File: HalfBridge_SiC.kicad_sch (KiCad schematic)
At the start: 0 parts

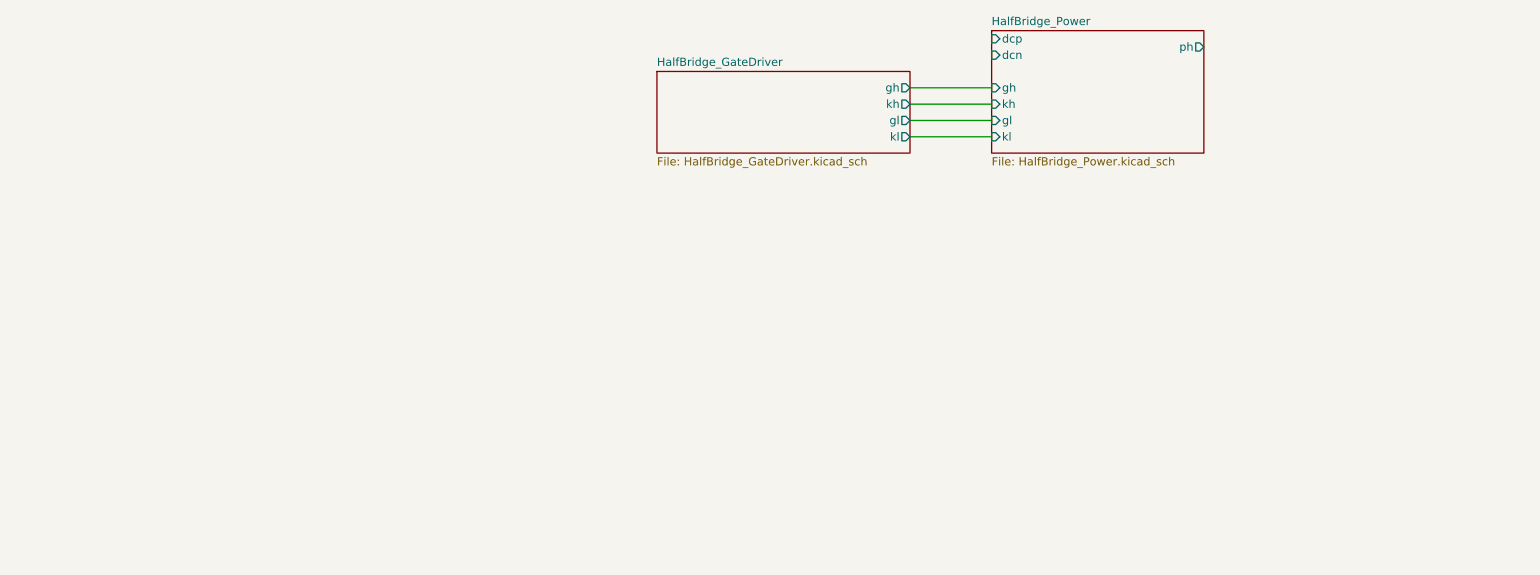
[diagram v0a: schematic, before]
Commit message: gate driver
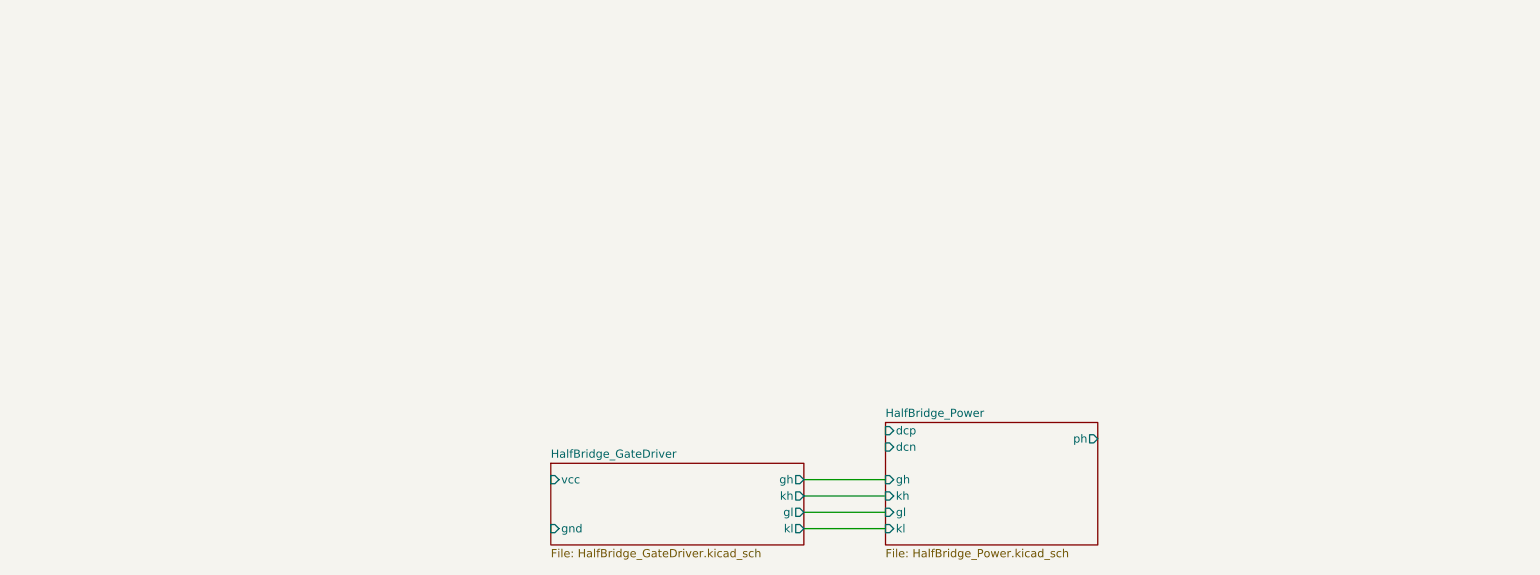
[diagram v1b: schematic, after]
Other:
- sheet HalfBridge_GateDriver ports: added gnd, vcc; removed none
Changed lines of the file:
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@@
 	(wire
 		(pts
-			(xy 132.08 63.5) (xy 144.78 63.5)
-		)
-		(stroke
-			(width 0)
-			(type default)
-		)
-	)
-	(wire
-		(pts
-			(xy 132.08 58.42) (xy 144.78 58.42)
-		)
-		(stroke
-			(width 0)
-			(type default)
-		)
-	)
-	(wire
-		(pts
-			(xy 132.08 60.96) (xy 144.78 60.96)
-		)
-		(stroke
-			(width 0)
-			(type default)
-		)
-	)
-	(wire
-		(pts
-			(xy 132.08 55.88) (xy 144.78 55.88)
+			(xy 115.57 124.46) (xy 128.27 124.46)
+		)
+		(stroke
+			(width 0)
+			(type default)
+		)
+	)
+	(wire
+		(pts
+			(xy 115.57 119.38) (xy 128.27 119.38)
+		)
+		(stroke
+			(width 0)
+			(type default)
+		)
+	)
+	(wire
+		(pts
+			(xy 115.57 121.92) (xy 128.27 121.92)
+		)
+		(stroke
+			(width 0)
+			(type default)
+		)
+	)
+	(wire
+		(pts
+			(xy 115.57 116.84) (xy 128.27 116.84)
 		)
 		(stroke
@@
 	)
 	(sheet
-		(at 92.71 53.34)
+		(at 76.2 114.3)
 		(size 39.37 12.7)
 		(fields_autoplaced yes)
@@
 		)
 		(property "Sheetname" "HalfBridge_GateDriver"
-			(at 92.71 52.6284 0)
+			(at 76.2 113.5884 0)
 			(effects
 				(font
@@
 		)
 		(property "Sheetfile" "HalfBridge_GateDriver.kicad_sch"
-			(at 92.71 66.6246 0)
+			(at 76.2 127.5846 0)
 			(effects
 				(font
@@
 		)
 		(pin "gl" output
-			(at 132.08 60.96 0)
+			(at 115.57 121.92 0)
 			(effects
 				(font
@@
 		)
 		(pin "kh" output
-			(at 132.08 58.42 0)
+			(at 115.57 119.38 0)
 			(effects
 				(font
@@
 		)
 		(pin "gh" output
-			(at 132.08 55.88 0)
+			(at 115.57 116.84 0)
 			(effects
 				(font
@@
 		)
 		(pin "kl" output
-			(at 132.08 63.5 0)
-			(effects
-				(font
-					(size 1.27 1.27)
-				)
-				(justify right)
+			(at 115.57 124.46 0)
+			(effects
+				(font
+					(size 1.27 1.27)
+				)
+				(justify right)
+			)
+		)
+		(pin "vcc" input
+			(at 76.2 116.84 180)
+			(effects
+				(font
+					(size 1.27 1.27)
+				)
+				(justify left)
+			)
+		)
+		(pin "gnd" input
+			(at 76.2 124.46 180)
+			(effects
+				(font
+					(size 1.27 1.27)
+				)
+				(justify left)
 			)
 		)
@@
 	)
 	(sheet
-		(at 144.78 46.99)
+		(at 128.27 107.95)
 		(size 33.02 19.05)
 		(fields_autoplaced yes)
@@
 		)
 		(property "Sheetname" "HalfBridge_Power"
-			(at 144.78 46.2784 0)
+			(at 128.27 107.2384 0)
 			(effects
 				(font
@@
 		)
 		(property "Sheetfile" "HalfBridge_Power.kicad_sch"
-			(at 144.78 66.6246 0)
+			(at 128.27 127.5846 0)
 			(effects
 				(font
@@
 		)
 		(pin "ph" output
-			(at 177.8 49.53 0)
+			(at 161.29 110.49 0)
 			(effects
 				(font
@@
 		)
 		(pin "dcp" input
-			(at 144.78 48.26 180)
+			(at 128.27 109.22 180)
 			(effects
 				(font
@@
 		)
 		(pin "dcn" input
-			(at 144.78 50.8 180)
+			(at 128.27 111.76 180)
 			(effects
 				(font
@@
 		)
 		(pin "gh" input
-			(at 144.78 55.88 180)
+			(at 128.27 116.84 180)
 			(effects
 				(font
@@
 		)
 		(pin "kh" input
-			(at 144.78 58.42 180)
+			(at 128.27 119.38 180)
 			(effects
 				(font
@@
 		)
 		(pin "gl" input
-			(at 144.78 60.96 180)
+			(at 128.27 121.92 180)
 			(effects
 				(font
@@
 		)
 		(pin "kl" input
-			(at 144.78 63.5 180)
-			(effects
-				(font
+			(at 128.27 124.46 180)
+			(effects
+				(font

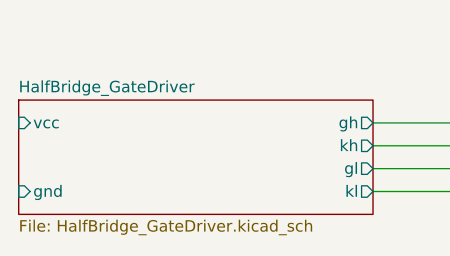
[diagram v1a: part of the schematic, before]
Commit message: symbol library gatedriver
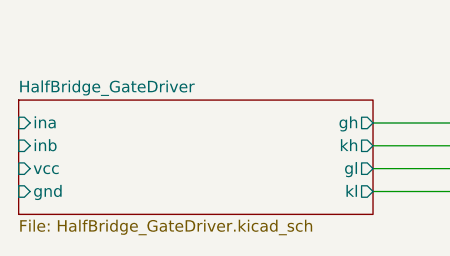
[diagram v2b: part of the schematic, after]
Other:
- sheet HalfBridge_GateDriver ports: added ina, inb; removed none
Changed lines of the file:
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@@
 		)
 		(pin "vcc" input
-			(at 76.2 116.84 180)
+			(at 76.2 121.92 180)
 			(effects
 				(font
@@
 			(effects
 				(font
+					(size 1.27 1.27)
+				)
+				(justify left)
+			)
+		)
+		(pin "ina" input
+			(at 76.2 116.84 180)
+			(effects
+				(font
+					(size 1.27 1.27)
+				)
+				(justify left)
+			)
+		)
+		(pin "inb" input
+			(at 76.2 119.38 180)
+			(effects
+				(font

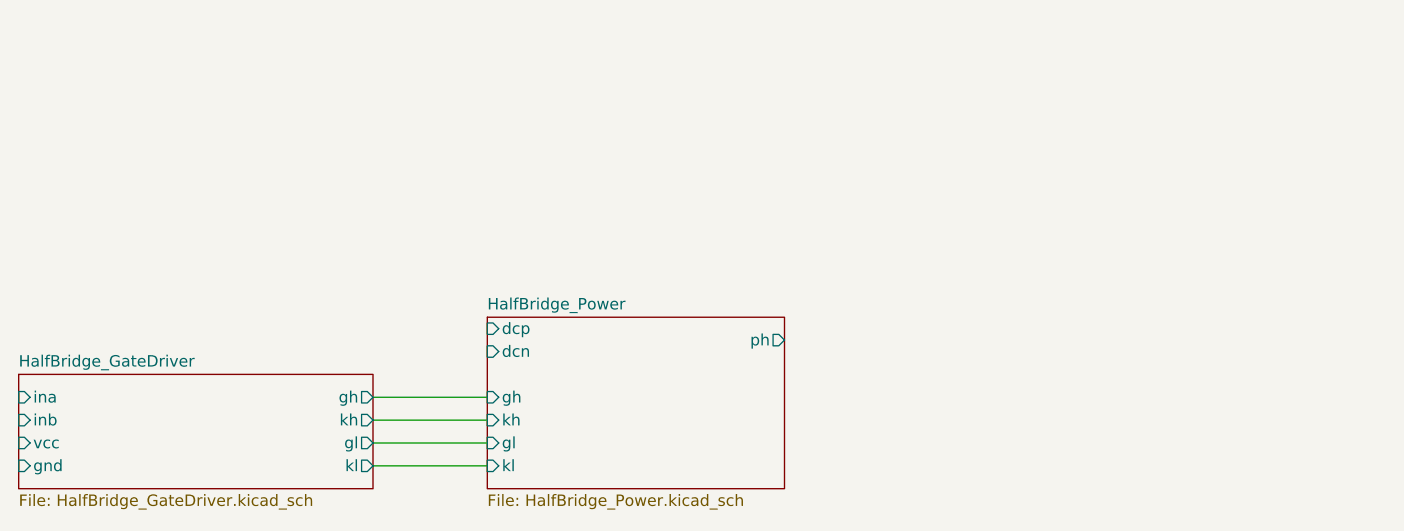
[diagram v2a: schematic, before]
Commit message: switch dpdt 3d model
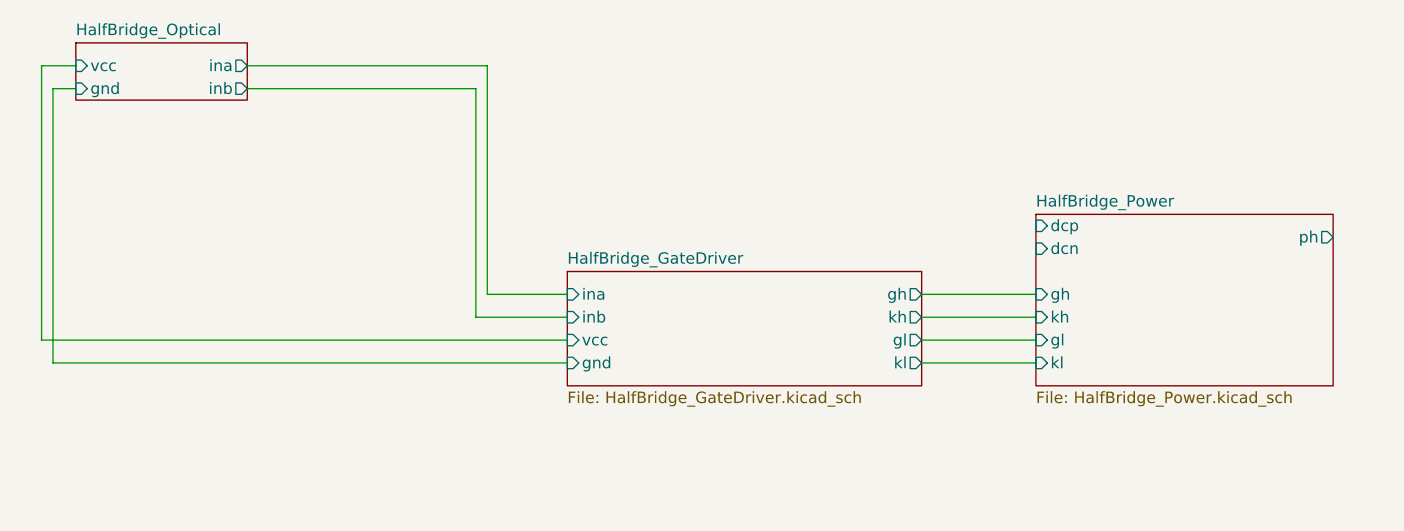
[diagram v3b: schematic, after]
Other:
- added sheet HalfBridge_Optical (HalfBridge_Optical.kicad_sch)
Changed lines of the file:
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@@
 	(wire
 		(pts
-			(xy 115.57 124.46) (xy 128.27 124.46)
-		)
-		(stroke
-			(width 0)
-			(type default)
-		)
-	)
-	(wire
-		(pts
-			(xy 115.57 119.38) (xy 128.27 119.38)
-		)
-		(stroke
-			(width 0)
-			(type default)
-		)
-	)
-	(wire
-		(pts
-			(xy 115.57 121.92) (xy 128.27 121.92)
-		)
-		(stroke
-			(width 0)
-			(type default)
-		)
-	)
-	(wire
-		(pts
-			(xy 115.57 116.84) (xy 128.27 116.84)
+			(xy 78.74 110.49) (xy 137.16 110.49)
+		)
+		(stroke
+			(width 0)
+			(type default)
+		)
+	)
+	(wire
+		(pts
+			(xy 176.53 113.03) (xy 189.23 113.03)
+		)
+		(stroke
+			(width 0)
+			(type default)
+		)
+	)
+	(wire
+		(pts
+			(xy 101.6 82.55) (xy 127 82.55)
+		)
+		(stroke
+			(width 0)
+			(type default)
+		)
+	)
+	(wire
+		(pts
+			(xy 176.53 107.95) (xy 189.23 107.95)
+		)
+		(stroke
+			(width 0)
+			(type default)
+		)
+	)
+	(wire
+		(pts
+			(xy 128.27 80.01) (xy 128.27 105.41)
+		)
+		(stroke
+			(width 0)
+			(type default)
+		)
+	)
+	(wire
+		(pts
+			(xy 101.6 80.01) (xy 128.27 80.01)
+		)
+		(stroke
+			(width 0)
+			(type default)
+		)
+	)
+	(wire
+		(pts
+			(xy 128.27 105.41) (xy 137.16 105.41)
+		)
+		(stroke
+			(width 0)
+			(type default)
+		)
+	)
+	(wire
+		(pts
+			(xy 82.55 80.01) (xy 78.74 80.01)
+		)
+		(stroke
+			(width 0)
+			(type default)
+		)
+	)
+	(wire
+		(pts
+			(xy 127 82.55) (xy 127 107.95)
+		)
+		(stroke
+			(width 0)
+			(type default)
+		)
+	)
+	(wire
+		(pts
+			(xy 80.01 82.55) (xy 80.01 113.03)
+		)
+		(stroke
+			(width 0)
+			(type default)
+		)
+	)
+	(wire
+		(pts
+			(xy 80.01 113.03) (xy 137.16 113.03)
+		)
+		(stroke
+			(width 0)
+			(type default)
+		)
+	)
+	(wire
+		(pts
+			(xy 127 107.95) (xy 137.16 107.95)
+		)
+		(stroke
+			(width 0)
+			(type default)
+		)
+	)
+	(wire
+		(pts
+			(xy 176.53 110.49) (xy 189.23 110.49)
+		)
+		(stroke
+			(width 0)
+			(type default)
+		)
+	)
+	(wire
+		(pts
+			(xy 82.55 82.55) (xy 80.01 82.55)
+		)
+		(stroke
+			(width 0)
+			(type default)
+		)
+	)
+	(wire
+		(pts
+			(xy 176.53 105.41) (xy 189.23 105.41)
+		)
+		(stroke
+			(width 0)
+			(type default)
+		)
+	)
+	(wire
+		(pts
+			(xy 78.74 80.01) (xy 78.74 110.49)
 		)
 		(stroke
@@
 	)
 	(sheet
-		(at 76.2 114.3)
+		(at 82.55 77.47)
+		(size 19.05 6.35)
+		(fields_autoplaced yes)
+		(stroke
+			(width 0.1524)
+			(type solid)
+		)
+		(fill
+			(color 0 0 0 0.0000)
+		)
+		(property "Sheetname" "HalfBridge_Optical"
+			(at 82.55 76.7584 0)
+			(effects
+				(font
+					(size 1.27 1.27)
+				)
+				(justify left bottom)
+			)
+		)
+		(property "Sheetfile" "HalfBridge_Optical.kicad_sch"
+			(at 82.55 84.4046 0)
+			(effects
+				(font
+					(size 1.27 1.27)
+				)
+				(justify left top)
+				(hide yes)
+			)
+		)
+		(pin "ina" output
+			(at 101.6 80.01 0)
+			(effects
+				(font
+					(size 1.27 1.27)
+				)
+				(justify right)
+			)
+		)
+		(pin "inb" output
+			(at 101.6 82.55 0)
+			(effects
+				(font
+					(size 1.27 1.27)
+				)
+				(justify right)
+			)
+		)
+		(pin "vcc" input
+			(at 82.55 80.01 180)
+			(effects
+				(font
+					(size 1.27 1.27)
+				)
+				(justify left)
+			)
+		)
+		(pin "gnd" input
+			(at 82.55 82.55 180)
+			(effects
+				(font
+					(size 1.27 1.27)
+				)
+				(justify left)
+			)
+		)
+		(instances
+			(project "HalfBridge_SiC"
+				(path "/3c187ffa-7f66-4861-b077-b6965c821fc2"
+					(page "4")
+				)
+			)
+		)
+	)
+	(sheet
+		(at 137.16 102.87)
 		(size 39.37 12.7)
 		(fields_autoplaced yes)
@@
 		)
 		(property "Sheetname" "HalfBridge_GateDriver"
-			(at 76.2 113.5884 0)
+			(at 137.16 102.1584 0)
 			(effects
 				(font
@@
 		)
 		(property "Sheetfile" "HalfBridge_GateDriver.kicad_sch"
-			(at 76.2 127.5846 0)
+			(at 137.16 116.1546 0)
 			(effects
 				(font
@@
 		)
 		(pin "gl" output
-			(at 115.57 121.92 0)
+			(at 176.53 110.49 0)
 			(effects
 				(font
@@
 		)
 		(pin "kh" output
-			(at 115.57 119.38 0)
+			(at 176.53 107.95 0)
 			(effects
 				(font
@@
 		)
 		(pin "gh" output
-			(at 115.57 116.84 0)
+			(at 176.53 105.41 0)
 			(effects
 				(font
@@
 		)
 		(pin "kl" output
-			(at 115.57 124.46 0)
+			(at 176.53 113.03 0)
 			(effects
 				(font
@@
 		)
 		(pin "vcc" input
-			(at 76.2 121.92 180)
+			(at 137.16 110.49 180)
 			(effects
 				(font
@@
 		)
 		(pin "gnd" input
-			(at 76.2 124.46 180)
+			(at 137.16 113.03 180)
 			(effects
 				(font
@@
 		)
 		(pin "ina" input
-			(at 76.2 116.84 180)
+			(at 137.16 105.41 180)
 			(effects
 				(font
@@
 		)
 		(pin "inb" input
-			(at 76.2 119.38 180)
+			(at 137.16 107.95 180)
 			(effects
 				(font
@@
 	)
 	(sheet
-		(at 128.27 107.95)
+		(at 189.23 96.52)
 		(size 33.02 19.05)
 		(fields_autoplaced yes)
@@
 		)
 		(property "Sheetname" "HalfBridge_Power"
-			(at 128.27 107.2384 0)
+			(at 189.23 95.8084 0)
 			(effects
 				(font
@@
 		)
 		(property "Sheetfile" "HalfBridge_Power.kicad_sch"
-			(at 128.27 127.5846 0)
+			(at 189.23 116.1546 0)
 			(effects
 				(font
@@
 		)
 		(pin "ph" output
-			(at 161.29 110.49 0)
+			(at 222.25 99.06 0)
 			(effects
 				(font
@@
 		)
 		(pin "dcp" input
-			(at 128.27 109.22 180)
+			(at 189.23 97.79 180)
 			(effects
 				(font
@@
 		)
 		(pin "dcn" input
-			(at 128.27 111.76 180)
+			(at 189.23 100.33 180)
 			(effects
 				(font
@@
 		)
 		(pin "gh" input
-			(at 128.27 116.84 180)
+			(at 189.23 105.41 180)
 			(effects
 				(font
@@
 		)
 		(pin "kh" input
-			(at 128.27 119.38 180)
+			(at 189.23 107.95 180)
 			(effects
 				(font
@@
 		)
 		(pin "gl" input
-			(at 128.27 121.92 180)
+			(at 189.23 110.49 180)
 			(effects
 				(font
@@
 		)
 		(pin "kl" input
-			(at 128.27 124.46 180)
-			(effects
-				(font
+			(at 189.23 113.03 180)
+			(effects
+				(font

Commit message: dc dc 3d
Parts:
- added D3: LED, LED_SMD:LED_0603_1608Metric_Pad1.05x0.95mm_HandSolder, symbol Device:LED
- added J4: Screw_Terminal_01x02, TerminalBlock_Phoenix:TerminalBlock_Phoenix_PT-1,5-2-3.5-H_1x02_P3.50mm_Horizontal, symbol Connector:Screw_Terminal_01x02
- added R17: R, Resistor_SMD:R_0603_1608Metric, symbol Device:R
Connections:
- net HalfBridge_GateDriver/gnd: now also J4.2 (Pin_2)
- net HalfBridge_GateDriver/vcc: now also D3.2 (A), J4.1 (Pin_1)
- new net: D3.1 (K), R17.1
- new net GND: R17.2

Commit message: position
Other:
- moved on the sheet: D3, J4, R17
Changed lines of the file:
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@@
 	(paper "A4")
 	(junction
-		(at 27.94 95.25)
+		(at 44.45 95.25)
 		(diameter 0)
 		(color 0 0 0 0)
@@
 	(wire
 		(pts
-			(xy 25.4 95.25) (xy 27.94 95.25)
-		)
-		(stroke
-			(width 0)
-			(type default)
-		)
-	)
-	(wire
-		(pts
-			(xy 27.94 109.22) (xy 27.94 111.76)
+			(xy 41.91 95.25) (xy 44.45 95.25)
+		)
+		(stroke
+			(width 0)
+			(type default)
+		)
+	)
+	(wire
+		(pts
+			(xy 44.45 109.22) (xy 44.45 111.76)
 		)
 		(stroke
@@
 	(wire
 		(pts
-			(xy 27.94 95.25) (xy 68.58 95.25)
+			(xy 44.45 95.25) (xy 68.58 95.25)
 		)
 		(stroke
@@
 	(wire
 		(pts
-			(xy 25.4 97.79) (xy 69.85 97.79)
+			(xy 41.91 97.79) (xy 69.85 97.79)
 		)
 		(stroke
@@
 	(wire
 		(pts
-			(xy 27.94 95.25) (xy 27.94 101.6)
+			(xy 44.45 95.25) (xy 44.45 101.6)
 		)
 		(stroke
@@
 	(symbol
 		(lib_id "Connector:Screw_Terminal_01x02")
-		(at 20.32 95.25 0)
+		(at 36.83 95.25 0)
 		(mirror y)
 		(unit 1)
@@
 		(dnp no)
 		(property "Reference" "J4"
-			(at 17.78 95.2499 0)
+			(at 34.29 95.2499 0)
 			(effects
 				(font
@@
 		)
 		(property "Value" "Screw_Terminal_01x02"
-			(at 17.78 97.7899 0)
+			(at 34.29 97.7899 0)
 			(effects
 				(font
@@
 		)
 		(property "Footprint" "TerminalBlock_Phoenix:TerminalBlock_Phoenix_PT-1,5-2-3.5-H_1x02_P3.50mm_Horizontal"
-			(at 20.32 95.25 0)
+			(at 36.83 95.25 0)
 			(effects
 				(font
@@
 		)
 		(property "Datasheet" "~"
-			(at 20.32 95.25 0)
+			(at 36.83 95.25 0)
 			(effects
 				(font
@@
 		)
 		(property "Description" "Generic screw terminal, single row, 01x02, script generated (kicad-library-utils/schlib/autogen/connector/)"
-			(at 20.32 95.25 0)
+			(at 36.83 95.25 0)
 			(effects
 				(font
@@
 	(symbol
 		(lib_id "Device:R")
-		(at 27.94 115.57 0)
+		(at 44.45 115.57 0)
 		(unit 1)
 		(exclude_from_sim no)
@@
 		(fields_autoplaced yes)
 		(property "Reference" "R17"
-			(at 30.48 114.2999 0)
+			(at 46.99 114.2999 0)
 			(effects
 				(font
@@
 		)
 		(property "Value" "R"
-			(at 30.48 116.8399 0)
+			(at 46.99 116.8399 0)
 			(effects
 				(font
@@
 		)
 		(property "Footprint" "Resistor_SMD:R_0603_1608Metric"
-			(at 26.162 115.57 90)
+			(at 42.672 115.57 90)
 			(effects
 				(font
@@
 		)
 		(property "Datasheet" "~"
-			(at 27.94 115.57 0)
+			(at 44.45 115.57 0)
 			(effects
 				(font
@@
 		)
 		(property "Description" "Resistor"
-			(at 27.94 115.57 0)
+			(at 44.45 115.57 0)
 			(effects
 				(font
@@
 	(symbol
 		(lib_id "Device:LED")
-		(at 27.94 105.41 90)
+		(at 44.45 105.41 90)
 		(unit 1)
 		(exclude_from_sim no)
@@
 		(fields_autoplaced yes)
 		(property "Reference" "D3"
-			(at 31.75 105.7274 90)
+			(at 48.26 105.7274 90)
 			(effects
 				(font
@@
 		)
 		(property "Value" "LED"
-			(at 31.75 108.2674 90)
+			(at 48.26 108.2674 90)
 			(effects
 				(font
@@
 		)
 		(property "Footprint" "LED_SMD:LED_0603_1608Metric_Pad1.05x0.95mm_HandSolder"
-			(at 27.94 105.41 0)
+			(at 44.45 105.41 0)
 			(effects
 				(font
@@
 		)
 		(property "Datasheet" "~"
-			(at 27.94 105.41 0)
+			(at 44.45 105.41 0)
 			(effects
 				(font
@@
 		)
 		(property "Description" "Light emitting diode"
-			(at 27.94 105.41 0)
+			(at 44.45 105.41 0)
 			(effects
 				(font
@@
 	(symbol
 		(lib_id "power:GND")
-		(at 27.94 119.38 0)
+		(at 44.45 119.38 0)
 		(unit 1)
 		(exclude_from_sim no)
@@
 		(fields_autoplaced yes)
 		(property "Reference" "#PWR01"
-			(at 27.94 125.73 0)
+			(at 44.45 125.73 0)
 			(effects
 				(font
@@
 		)
 		(property "Value" "GND"
-			(at 27.94 124.46 0)
+			(at 44.45 124.46 0)
 			(effects
 				(font
@@
 		)
 		(property "Footprint" ""
-			(at 27.94 119.38 0)
+			(at 44.45 119.38 0)
 			(effects
 				(font
@@
 		)
 		(property "Datasheet" ""
-			(at 27.94 119.38 0)
+			(at 44.45 119.38 0)
 			(effects
 				(font
@@
 		)
 		(property "Description" "Power symbol creates a global label with name \"GND\" , ground"
-			(at 27.94 119.38 0)
-			(effects
-				(font
+			(at 44.45 119.38 0)
+			(effects
+				(font

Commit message: diff rx
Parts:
- added SW2: CAS-D20X1, My_Button_Switch_SMD:Nidec_Copal_CAS-D20A1, symbol My_Switch:CAS-D20X1
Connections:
- net HalfBridge_GateDriver/ina: now also SW2.2 (B)
- net HalfBridge_GateDriver/inb: now also SW2.5 (B)
- net HalfBridge_GateDriver/gnd renamed HalfBridge_Diff/gnd
- net HalfBridge_GateDriver/vcc renamed HalfBridge_Diff/vcc
- new net HalfBridge_Diff/ina_d: SW2.1 (A)
- new net HalfBridge_Diff/inb_d: SW2.4 (A)
- new net HalfBridge_Optical/ina: SW2.3 (C)
- new net HalfBridge_Optical/inb: SW2.6 (C)
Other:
- added sheet HalfBridge_Diff (HalfBridge_Diff.kicad_sch)
